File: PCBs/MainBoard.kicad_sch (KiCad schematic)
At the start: 55 parts, among them J1 USB_C_Receptacle, J2 Conn_01x12_FPC_0.5mm, J3 Conn_01x08, J4 Qwiic_RA, SW1 PTH_RA_h7.5mm, SW2 SMD_4.6x2.8mm_h2.5mm, SW3 SMD_4.6x2.8mm_h2.5mm, U1 TVS_ESD_USB, U2 ESP32-S3-MINI, U3 AP3012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

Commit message: Screen and Main Board Updates
Updated Main board to Screen PCB connection, added accelerometer to Epaper display PCB. Removed GPIO 0 PB and replaced external Reset button with GPIO0 button.
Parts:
- removed SW3: SMD_4.6x2.8mm_h2.5mm, SparkFun-Switch:Momentary_SMD_4.6x2.8mm_h2.5mm, symbol SparkFun-Switch:SPST_Momentary_SMD_4.6x2.8mm_h2.5mm
- added D4: Red, SparkFun-LED:LED_0603_1608Metric, symbol SparkFun-LED:LED_Red_0603
- added R15: 220_0603, SparkFun-Resistor:R_0603_1608Metric, symbol SparkFun-Resistor:220_0603
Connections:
- net ESP0: now also SW1.2 (B)
- net GND: now also D4.1 (K)
- net RESET: no longer SW1.2 (B)
- net SCL: now also J2.9 (Pin_9)
- net SDA: now also J2.10 (Pin_10)
- net ESP DBG: now reaches U2.30 (IO48)
- net ESP DBG: now also R15.1
- new net: D4.2 (A), R15.2
- no-connect marks 31 -> 28
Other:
- note added: "EXTERNAL GPIO0 BUTTON"
- note removed: "EXTERNAL RESET BUTTON"
- note removed: "GPIO/BOOT BUTTON"
- moved on the sheet: J4, R10, R11, R13, R14, R7, R8, U4, U7

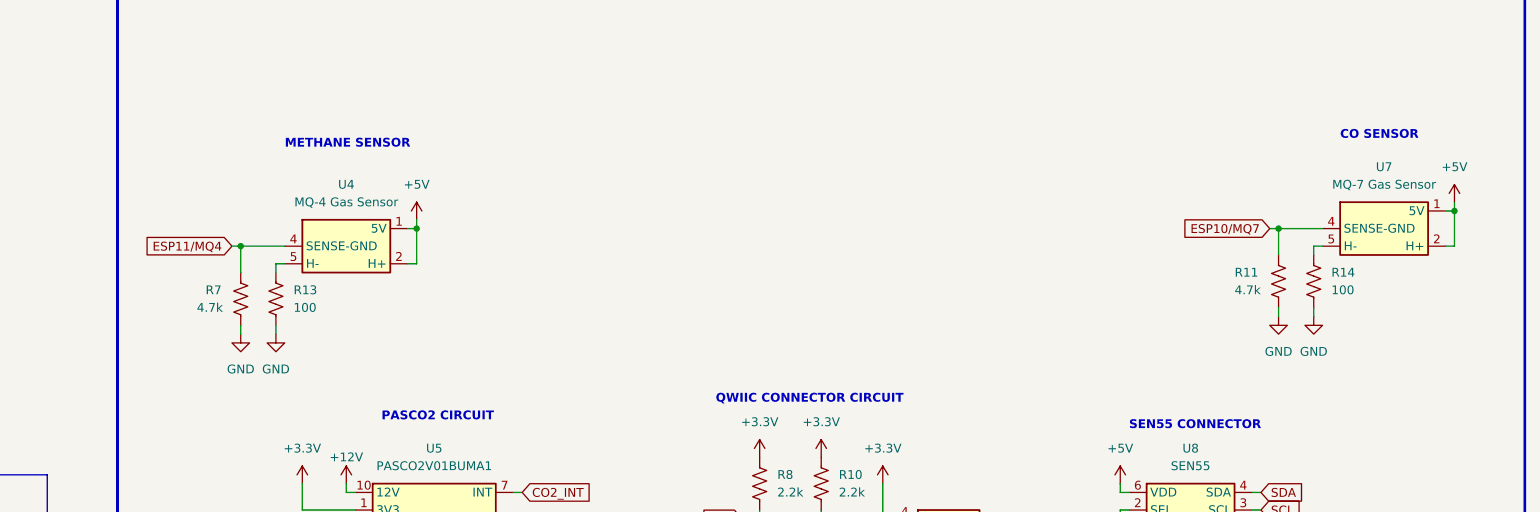
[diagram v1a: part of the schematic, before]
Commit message: Updated Main Board PCB
Removed H- resistors to GND from schematic and PCB after confirmed testing that we don't need them.
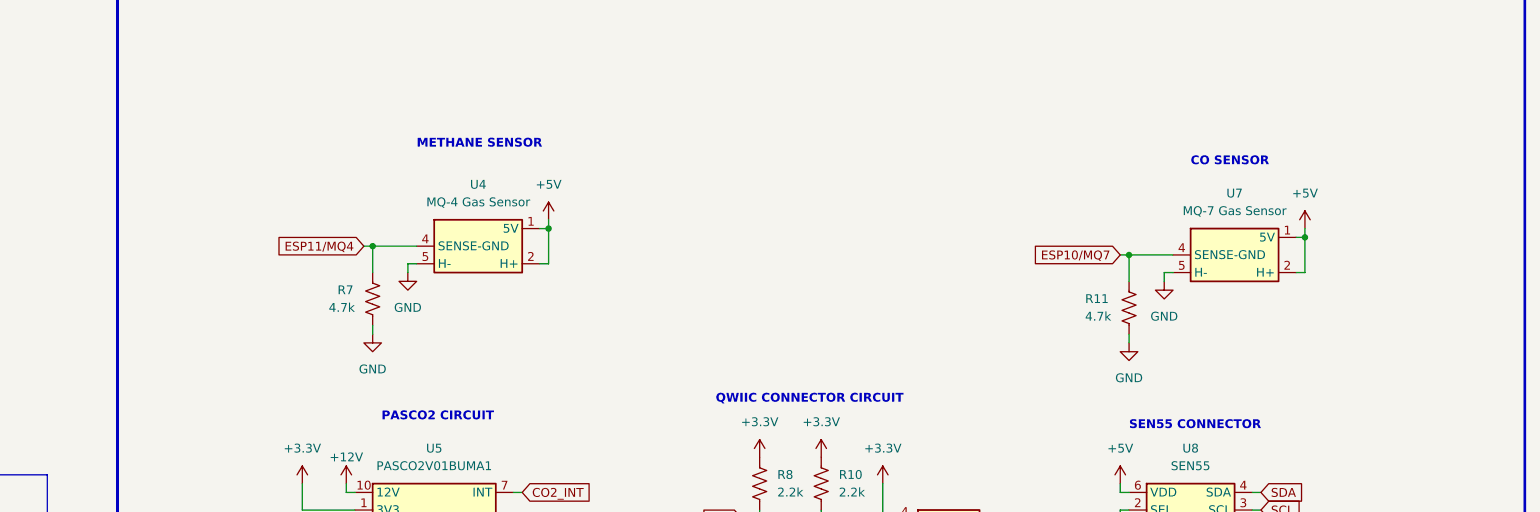
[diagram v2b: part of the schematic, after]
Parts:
- removed R13, R14: 100, SparkFun-Resistor:R_0603_1608Metric, symbol SparkFun-Resistor:100_0603
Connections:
- net GND: now also U4.5 (H-), U7.5 (H-)
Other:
- moved on the sheet: R11, R7, U4, U7

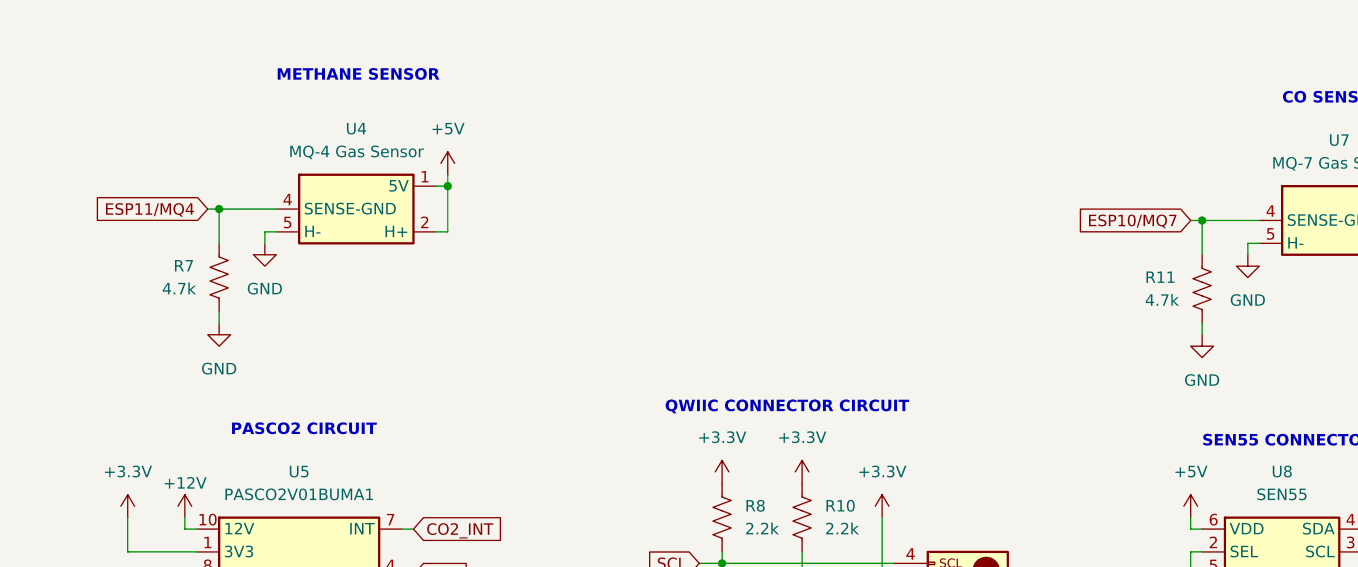
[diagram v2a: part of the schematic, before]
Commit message: Update Main Board V13.4
Replaced resistor on MQ sensor for resistor that is said to use on data sheet. from 4.7k ohm to 10k ohm.
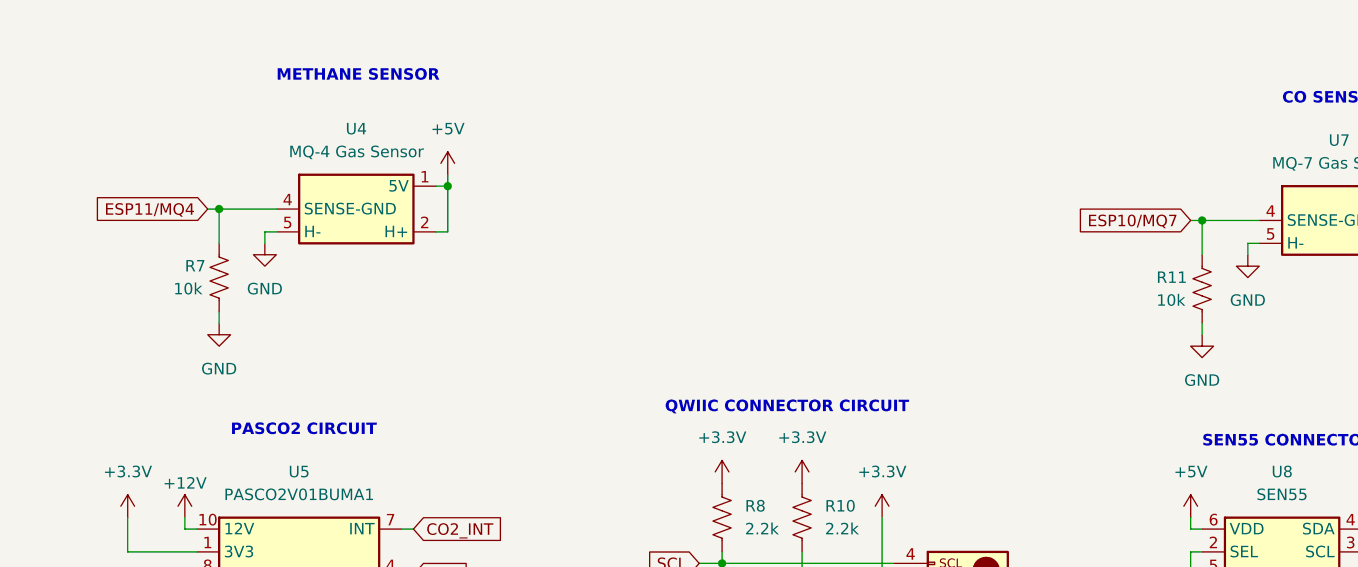
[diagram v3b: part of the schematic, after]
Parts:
- removed R11, R7: 4.7k, SparkFun-Resistor:R_0603_1608Metric, symbol SparkFun-Resistor:4.7k_0603
- added R11, R7: 10k, SparkFun-Resistor:R_0603_1608Metric, symbol SparkFun-Resistor:10k_0603
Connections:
- net ESP10/MQ7: now also R11.1
- net GND: now also R11.2, R7.2
- net SENSE-GND: now also R7.1
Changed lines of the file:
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@@
   (title_block
     (title "SparkFun Home Air Quality Sensor - Main PCB")
-    (rev "V13.3")
+    (rev "V13.4")
     (comment 1 "Designed By : Anton Vandenberge")
   )
@@
     )
   )
-  (symbol (lib_id "SparkFun-Resistor:4.7k_0603") (at 350.52 157.48 90) (unit 1)
-    (in_bom yes) (on_board yes) (dnp no)
-    (property "Reference" "R11" (at 344.17 156.21 90)
-      (effects (font (size 1.27 1.27)) (justify right))
-    )
-    (property "Value" "4.7k" (at 344.17 158.75 90)
-      (effects (font (size 1.27 1.27)) (justify right))
-    )
-    (property "Footprint" "SparkFun-Resistor:R_0603_1608Metric" (at 354.838 157.48 0)
-      (effects (font (size 1.27 1.27)) hide)
-    )
-    (property "Datasheet" "https://www.vishay.com/docs/20035/dcrcwe3.pdf" (at 359.41 157.48 0)
-      (effects (font (size 1.27 1.27)) hide)
-    )
-    (property "PROD_ID" "RES-07857" (at 357.124 157.48 0)
-      (effects (font (size 1.27 1.27)) hide)
-    )
-    (pin "1")
-    (pin "2")
-    (instances
-      (project "MainBoard"
-        (path "/70111962-74ad-442f-8642-d12c4115fcfb"
-          (reference "R11") (unit 1)
-        )
-      )
-    )
-  )
   (symbol (lib_id "power:GND") (at 62.23 78.74 0) (unit 1)
     (in_bom yes) (on_board yes) (dnp no)
@@
         (path "/70111962-74ad-442f-8642-d12c4115fcfb"
           (reference "FID4") (unit 1)
-        )
-      )
-    )
-  )
-  (symbol (lib_id "SparkFun-Resistor:4.7k_0603") (at 241.3 156.21 90) (unit 1)
-    (in_bom yes) (on_board yes) (dnp no)
-    (property "Reference" "R7" (at 236.22 154.94 90)
-      (effects (font (size 1.27 1.27)) (justify right))
-    )
-    (property "Value" "4.7k" (at 234.95 157.48 90)
-      (effects (font (size 1.27 1.27)) (justify right))
-    )
-    (property "Footprint" "SparkFun-Resistor:R_0603_1608Metric" (at 245.618 156.21 0)
-      (effects (font (size 1.27 1.27)) hide)
-    )
-    (property "Datasheet" "https://www.vishay.com/docs/20035/dcrcwe3.pdf" (at 250.19 156.21 0)
-      (effects (font (size 1.27 1.27)) hide)
-    )
-    (property "PROD_ID" "RES-07857" (at 247.904 156.21 0)
-      (effects (font (size 1.27 1.27)) hide)
-    )
-    (pin "1")
-    (pin "2")
-    (instances
-      (project "MainBoard"
-        (path "/70111962-74ad-442f-8642-d12c4115fcfb"
-          (reference "R7") (unit 1)
         )
       )
@@
     )
   )
+  (symbol (lib_id "SparkFun-Resistor:10k_0603") (at 350.52 157.48 90) (unit 1)
+    (in_bom yes) (on_board yes) (dnp no)
+    (property "Reference" "R11" (at 345.44 156.21 90)
+      (effects (font (size 1.27 1.27)) (justify right))
+    )
+    (property "Value" "10k" (at 345.44 158.75 90)
+      (effects (font (size 1.27 1.27)) (justify right))
+    )
+    (property "Footprint" "SparkFun-Resistor:R_0603_1608Metric" (at 354.838 157.48 0)
+      (effects (font (size 1.27 1.27)) hide)
+    )
+    (property "Datasheet" "https://www.vishay.com/docs/20035/dcrcwe3.pdf" (at 358.14 157.48 0)
+      (effects (font (size 1.27 1.27)) hide)
+    )
+    (property "PROD_ID" "RES-00824" (at 356.87 157.48 0)
+      (effects (font (size 1.27 1.27)) hide)
+    )
+    (pin "1")
+    (pin "2")
+    (instances
+      (project "MainBoard"
+        (path "/70111962-74ad-442f-8642-d12c4115fcfb"
+          (reference "R11") (unit 1)
+        )
+      )
+    )
+  )
   (symbol (lib_id "SparkFun-Resistor:2.2k_0603") (at 297.18 182.88 90) (unit 1)
     (in_bom yes) (on_board yes) (dnp no) (fields_autoplaced)
@@
         )
       )
+    )
+  )
+  (symbol (lib_id "SparkFun-Resistor:10k_0603") (at 241.3 156.21 90) (unit 1)
+    (in_bom yes) (on_board yes) (dnp no)
+    (property "Reference" "R7" (at 237.49 154.94 90)
+      (effects (font (size 1.27 1.27)) (justify right))
+    )
+    (property "Value" "10k" (at 236.22 157.48 90)
+      (effects (font (size 1.27 1.27)) (justify right))
+    )
+    (property "Footprint" "SparkFun-Resistor:R_0603_1608Metric" (at 245.618 156.21 0)
+      (effects (font (size 1.27 1.27)) hide)
+    )
+    (property "Datasheet" "https://www.vishay.com/docs/20035/dcrcwe3.pdf" (at 248.92 156.21 0)
+      (effects (font (size 1.27 1.27)) hide)
+    )
+    (property "PROD_ID" "RES-00824" (at 247.65 156.21 0)
+      (effects (font (size 1.27 1.27)) hide)
+    )
+    (pin "1")
+    (pin "2")
+    (instances
+      (project "MainBoard"
+        (path "/70111962-74ad-442f-8642-d12c4115fcfb"
+          (reference "R7") (unit 1)
+        )
+      )

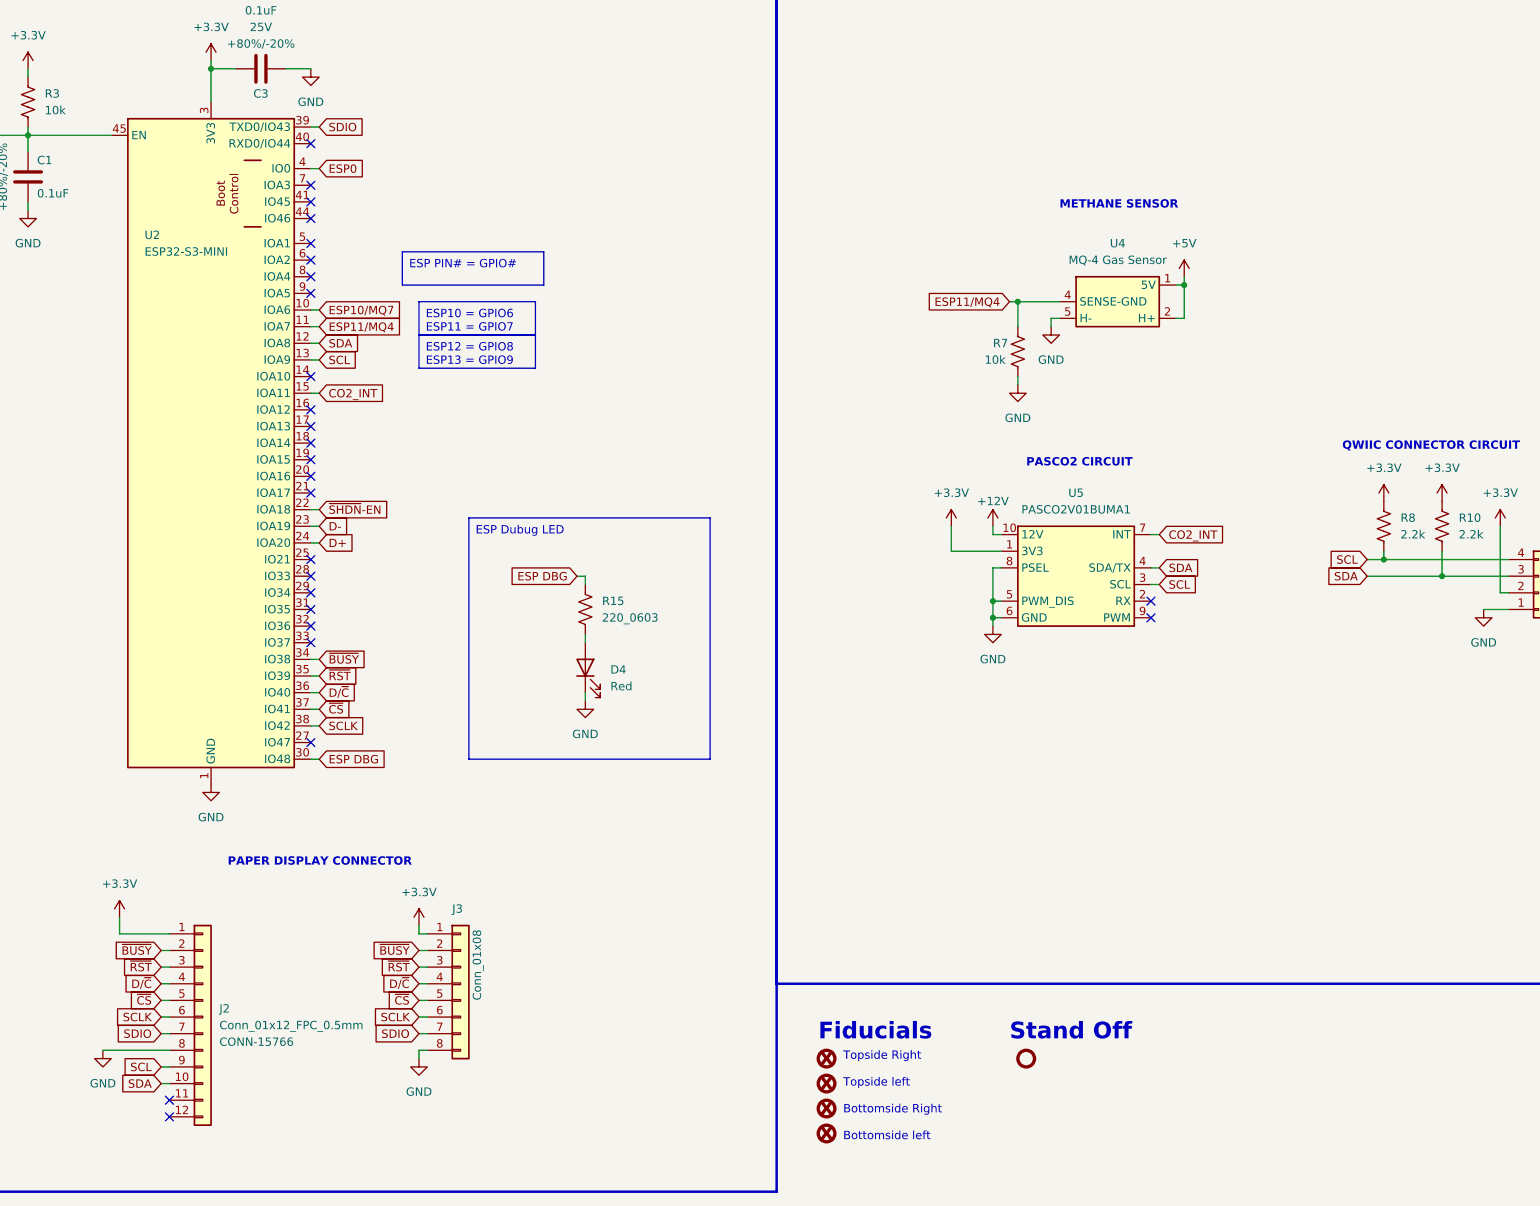
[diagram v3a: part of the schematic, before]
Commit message: Adding updates From review
Fixed epaper to main board FPC connection.
Added fiducials to main board for stencil alignment purposes.
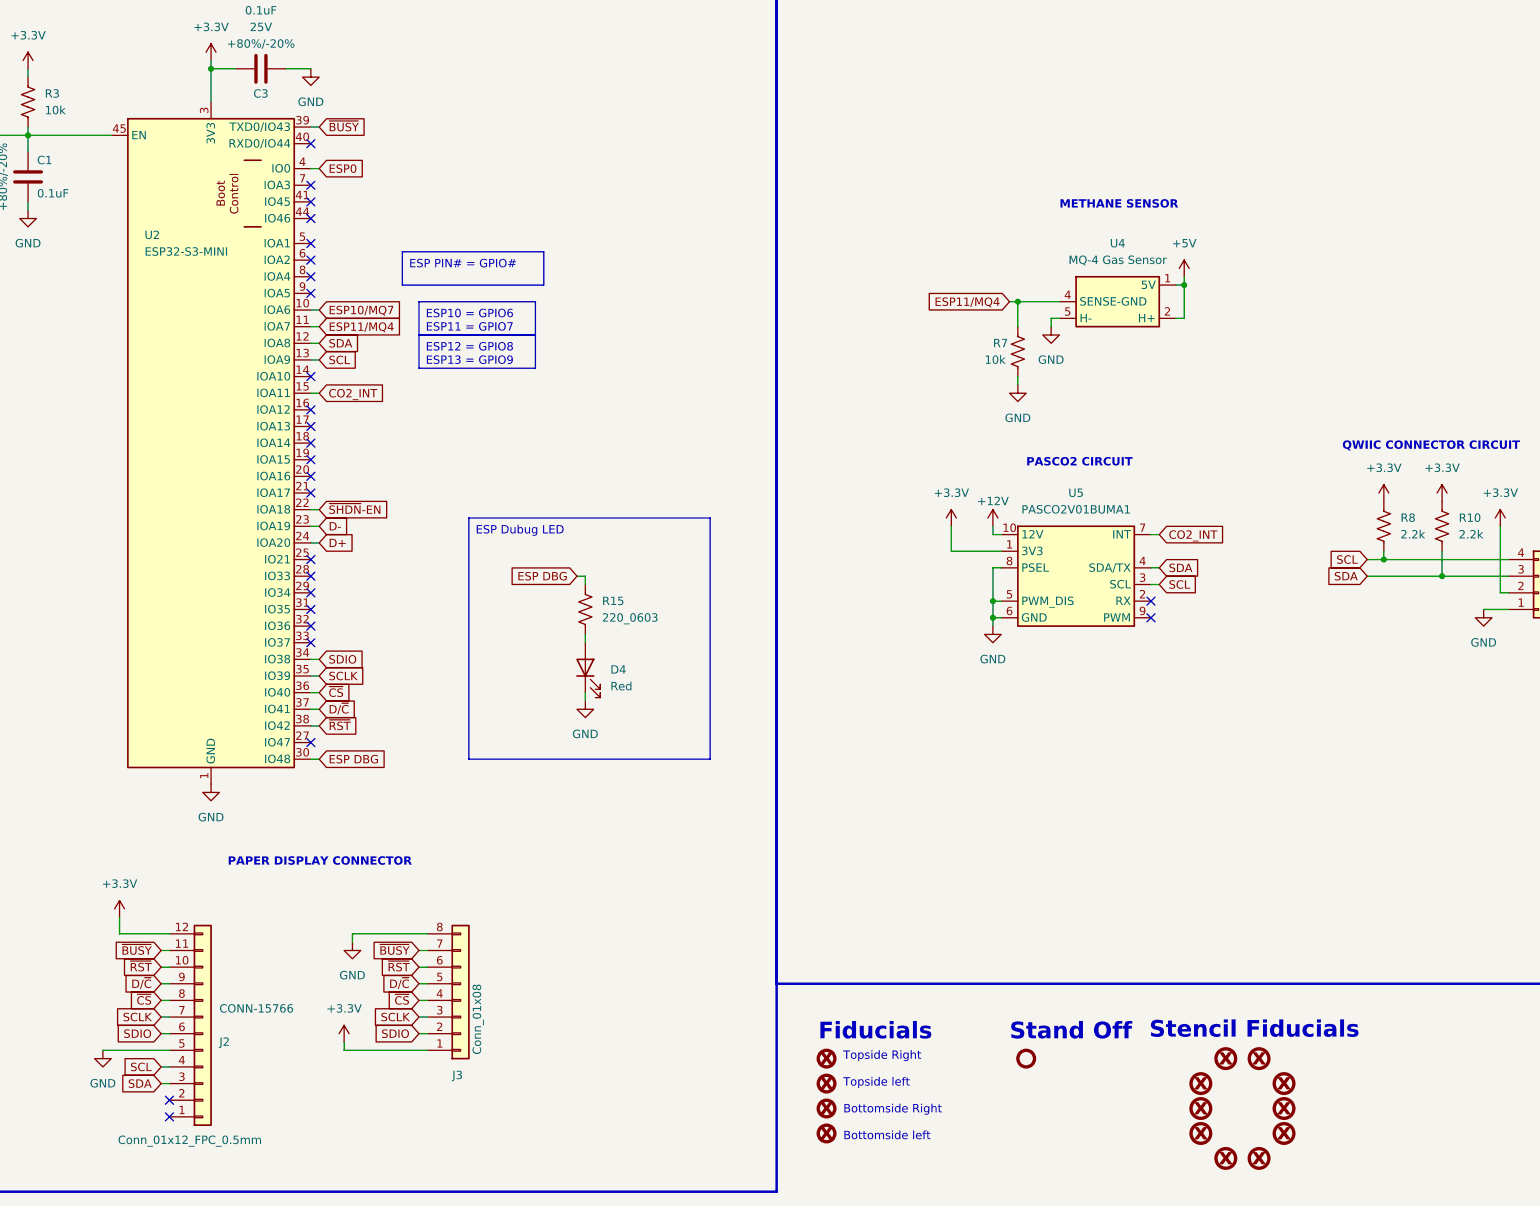
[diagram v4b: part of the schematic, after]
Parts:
- added FID10, FID11, FID12, FID13, FID14, FID5, FID6, FID7, FID8, FID9: Fiducial_3mm, SparkFun-Aesthetic:Fiducial_1.5mm_Mask3mm, symbol SparkFun-Aesthetic:Fiducial_3mm
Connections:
- net +3.3V: now also J2.12 (Pin_12); no longer J2.1 (Pin_1)
- net D/~{C}: now also J2.9 (Pin_9), J3.5 (Pin_5), U2.37 (IO41); no longer J2.4 (Pin_4), J3.4 (Pin_4), U2.36 (IO40)
- net GND: now also J2.5 (Pin_5); no longer J2.8 (Pin_8)
- net SCL: now also J2.4 (Pin_4); no longer J2.9 (Pin_9)
- net SCLK: now also J2.7 (Pin_7), J3.3 (Pin_3), U2.35 (IO39); no longer J2.6 (Pin_6), J3.6 (Pin_6), U2.38 (IO42)
- net SDA: now also J2.3 (Pin_3); no longer J2.10 (Pin_10)
- net SDIO: now also J2.6 (Pin_6), J3.2 (Pin_2), U2.34 (IO38); no longer J2.7 (Pin_7), J3.7 (Pin_7), U2.39 (TXD0/IO43)
- net ~{BUSY}: now also J2.11 (Pin_11), J3.7 (Pin_7), U2.39 (TXD0/IO43); no longer J2.2 (Pin_2), J3.2 (Pin_2), U2.34 (IO38)
- net ~{CS}: now also J2.8 (Pin_8), J3.4 (Pin_4), U2.36 (IO40); no longer J2.5 (Pin_5), J3.5 (Pin_5), U2.37 (IO41)
- net ~{RST}: now also J2.10 (Pin_10), J3.6 (Pin_6), U2.38 (IO42); no longer J2.3 (Pin_3), J3.3 (Pin_3), U2.35 (IO39)
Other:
- note added: "Stencil Fiducials"
